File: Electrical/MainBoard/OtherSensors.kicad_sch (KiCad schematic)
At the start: 26 parts, among them J10 Refl_Mount, J11 Refl_Mount, J12 Refl_Mount, J13 Refl_PCB_Connect, J14 Refl_PCB_Connect, J15 Refl_PCB_Connect, K1 QRE1113GR, K2 QRE1113GR, K3 QRE1113GR, SW10 SW_SPST, SW7 SW_SPST, SW8 SW_SPST, SW9 SW_SPST

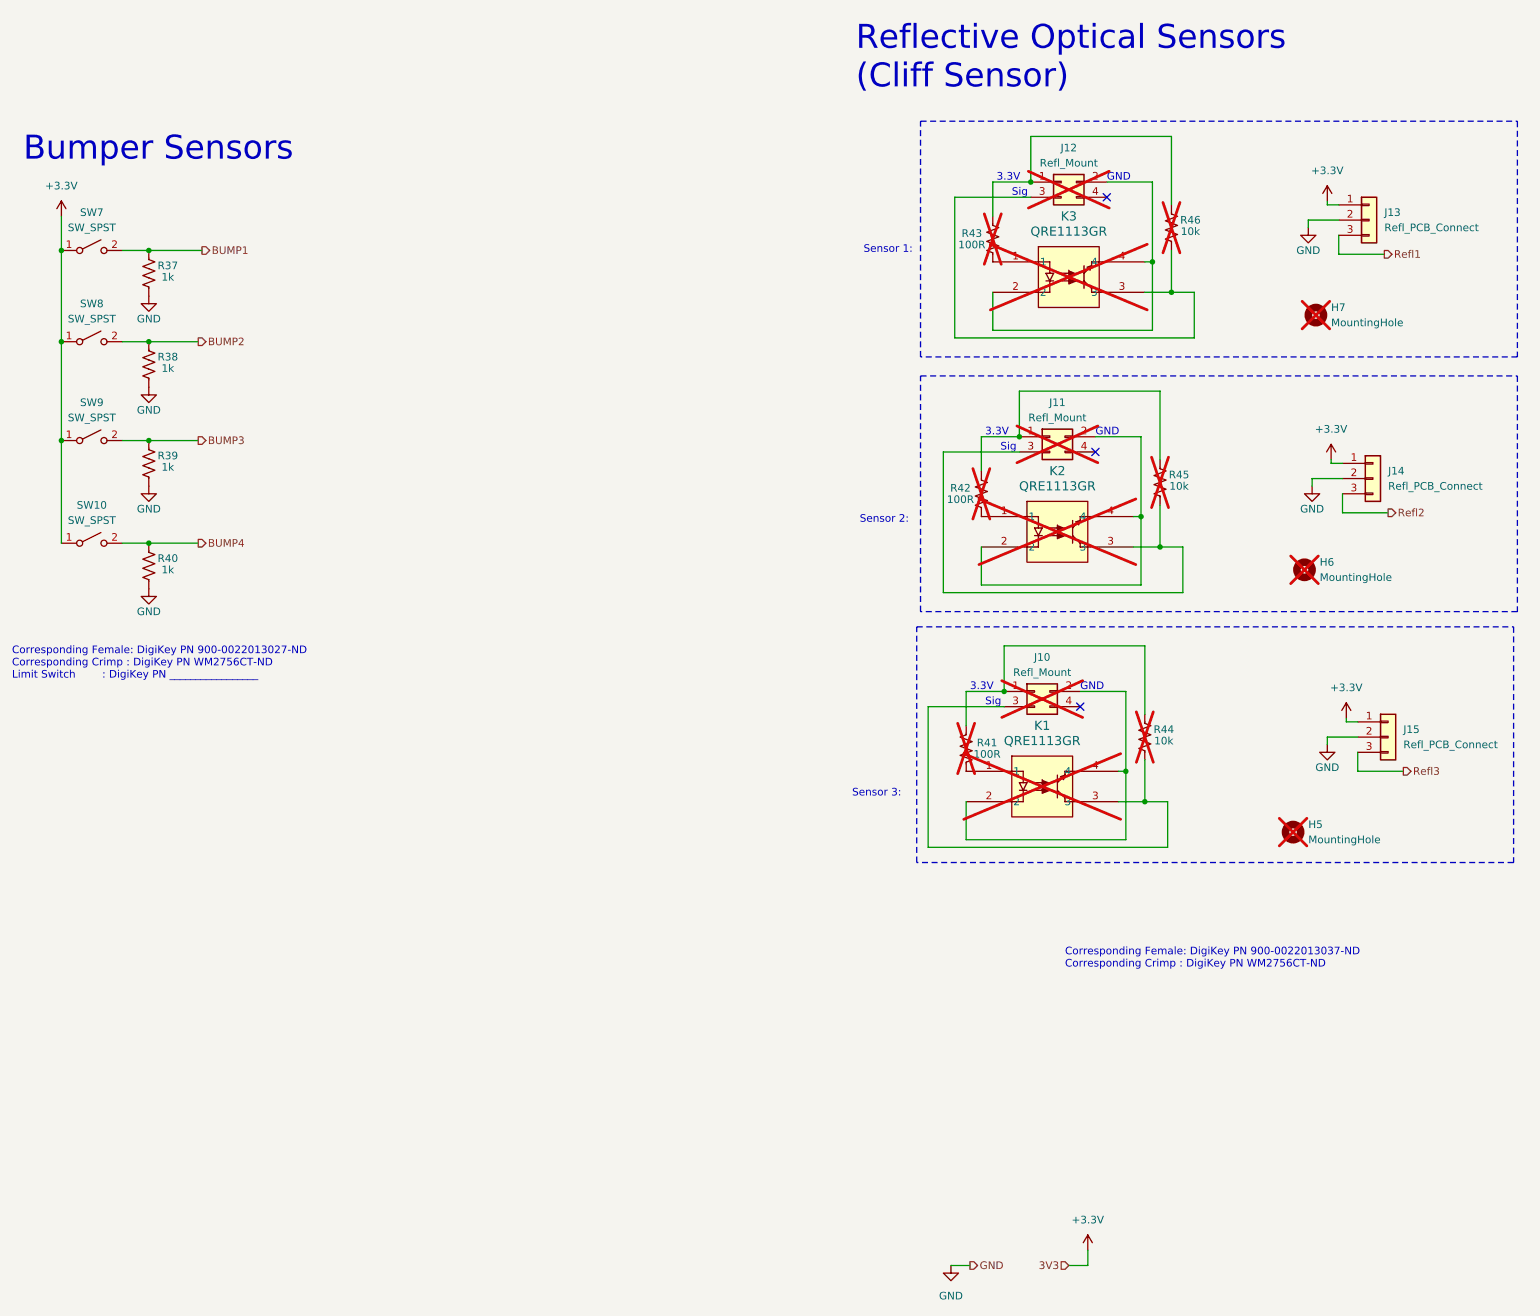
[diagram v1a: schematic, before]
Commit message: Use more molex picoblades and make schematic prettier
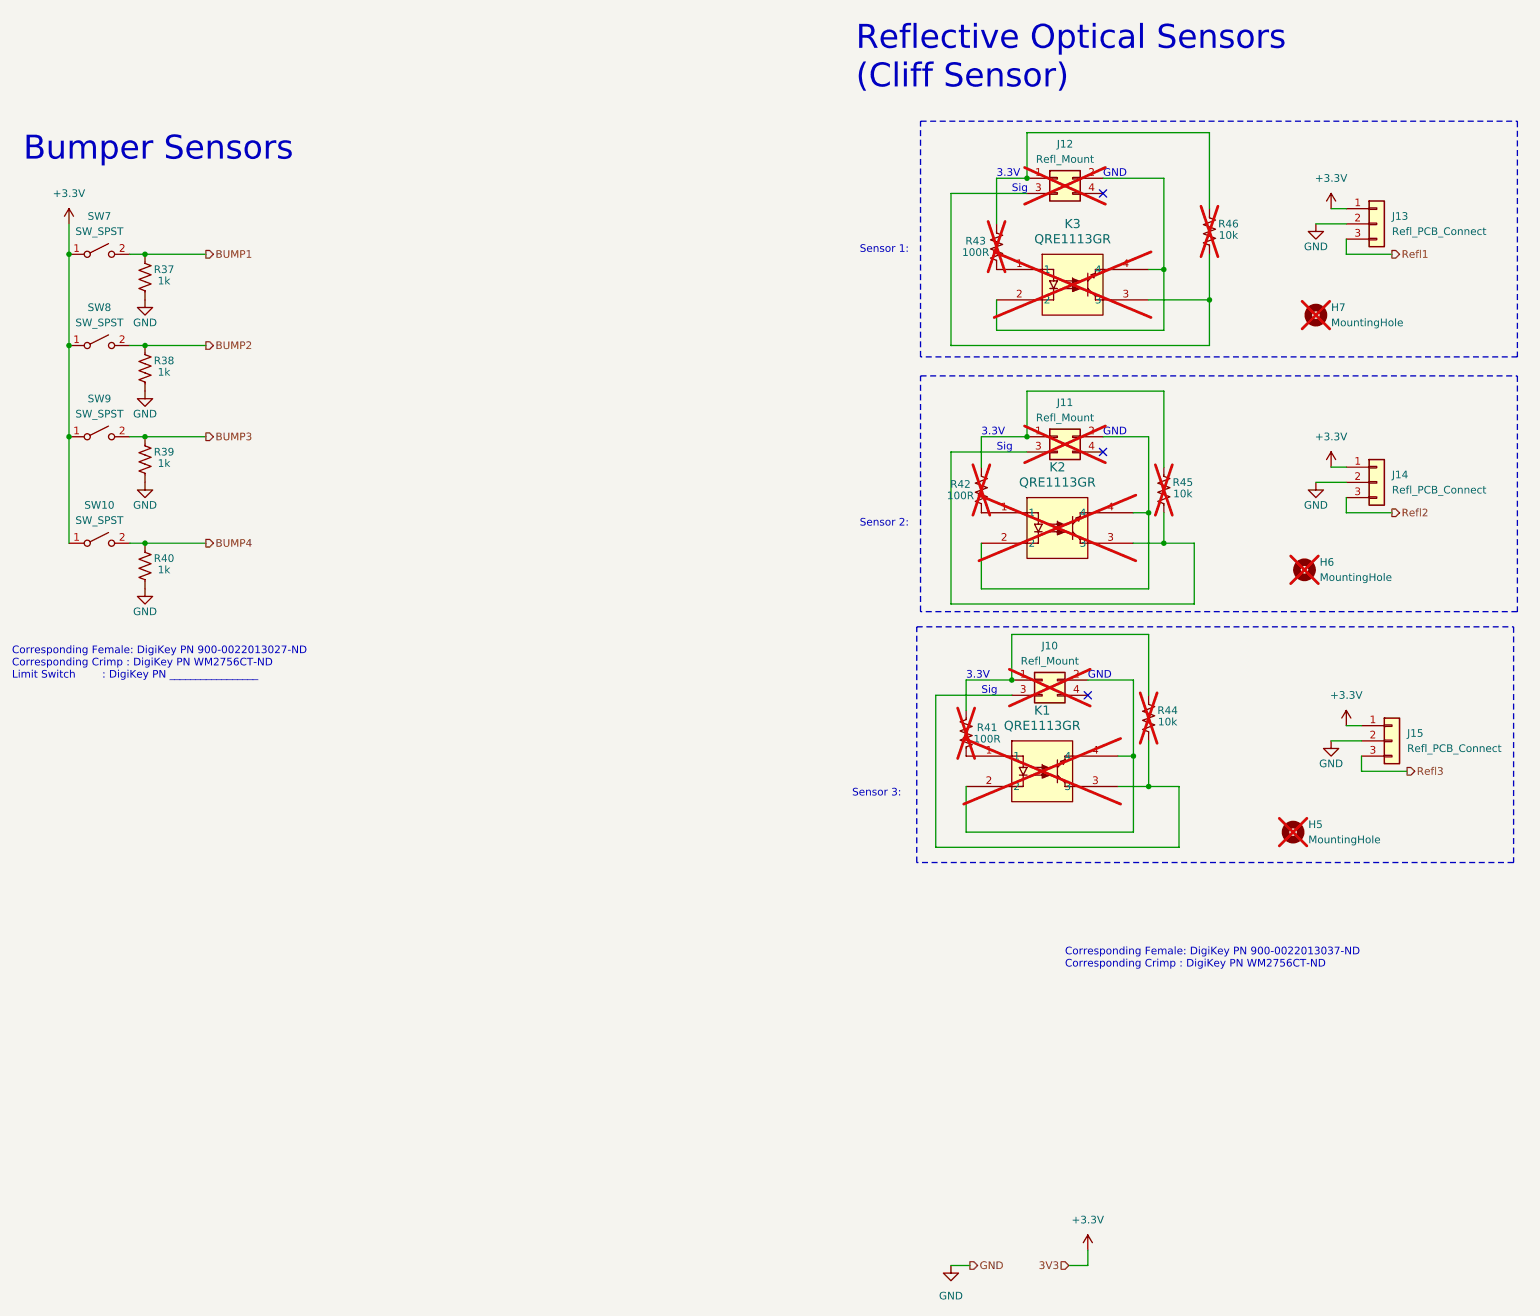
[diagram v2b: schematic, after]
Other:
- moved on the sheet: J10, J11, J12, J13, J14, J15, K1, K2, K3, R37, R38, R39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
